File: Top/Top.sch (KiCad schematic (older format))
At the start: 30 parts, among them J1 Conn_01x02_Male, SW1 SW_DPDT_x2, U2 MCP73831-2-OT, U3 SSD1306

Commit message: V0.2: Redo front schematic and PCB
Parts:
- removed H6: VBS, Custom:Mounting_Pad_Power, symbol Custom:MountingPad
- removed SW1: SW_DPDT_x2, Custom:JS102011SAQN, symbol Switch:SW_DPDT_x2
- H12, H13: value VBS -> PWR
- H2: value VSW -> PWR
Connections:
- net VBAT_SWITCH is gone; now on net VBUS: D1.1 (K), H2.1 (Pin)
- net +BATT: now also D1.2 (A)
- no-connect marks 1 -> 0
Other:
- note added: "Iref determines brightness"
- moved on the sheet: C2, D1, D2, H1, H10, H11, H12, H13, H2, H7, H8, H9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

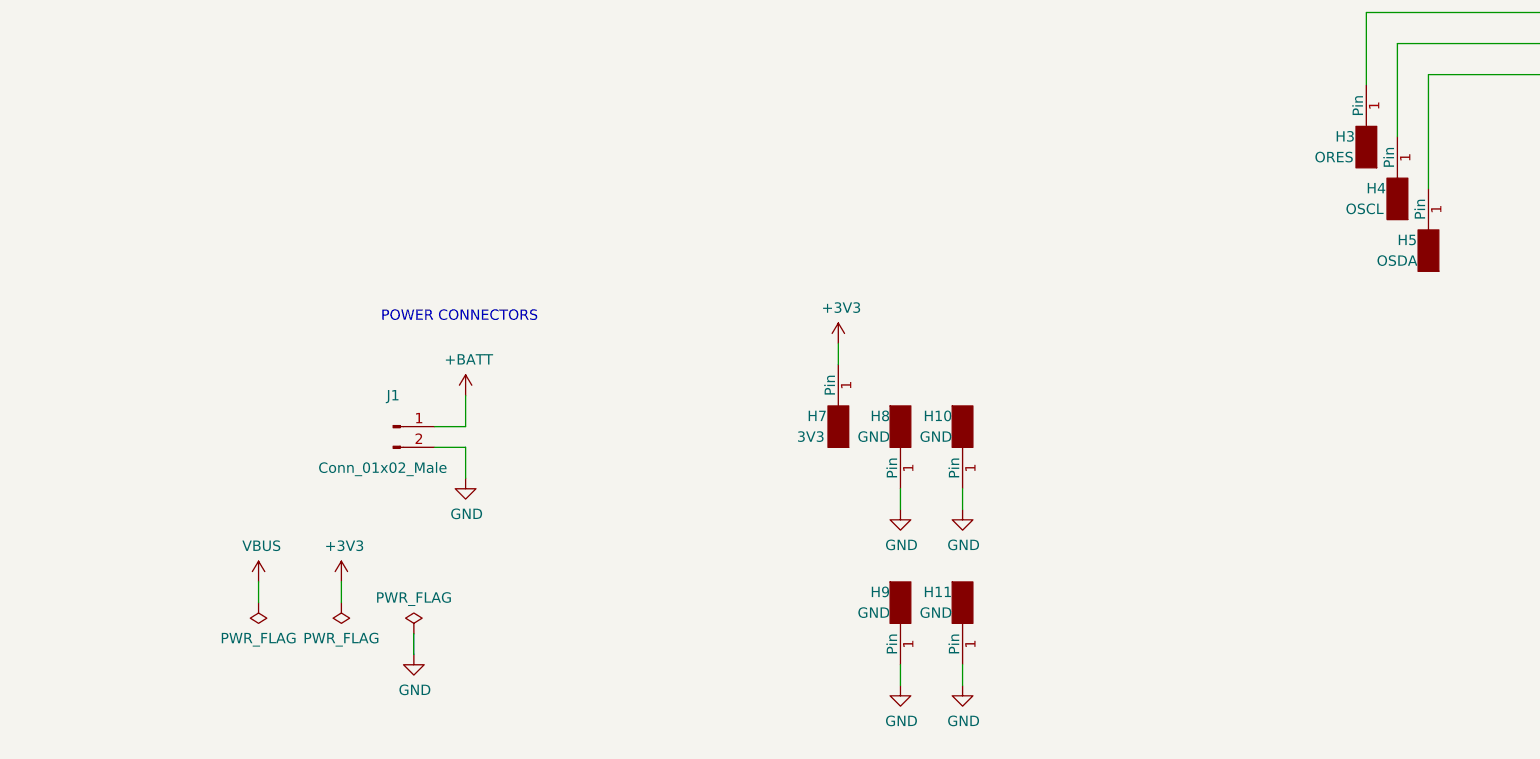
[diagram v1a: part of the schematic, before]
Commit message: updated bottom (motor placement, sharp sensor), front redesign, start op top redesign
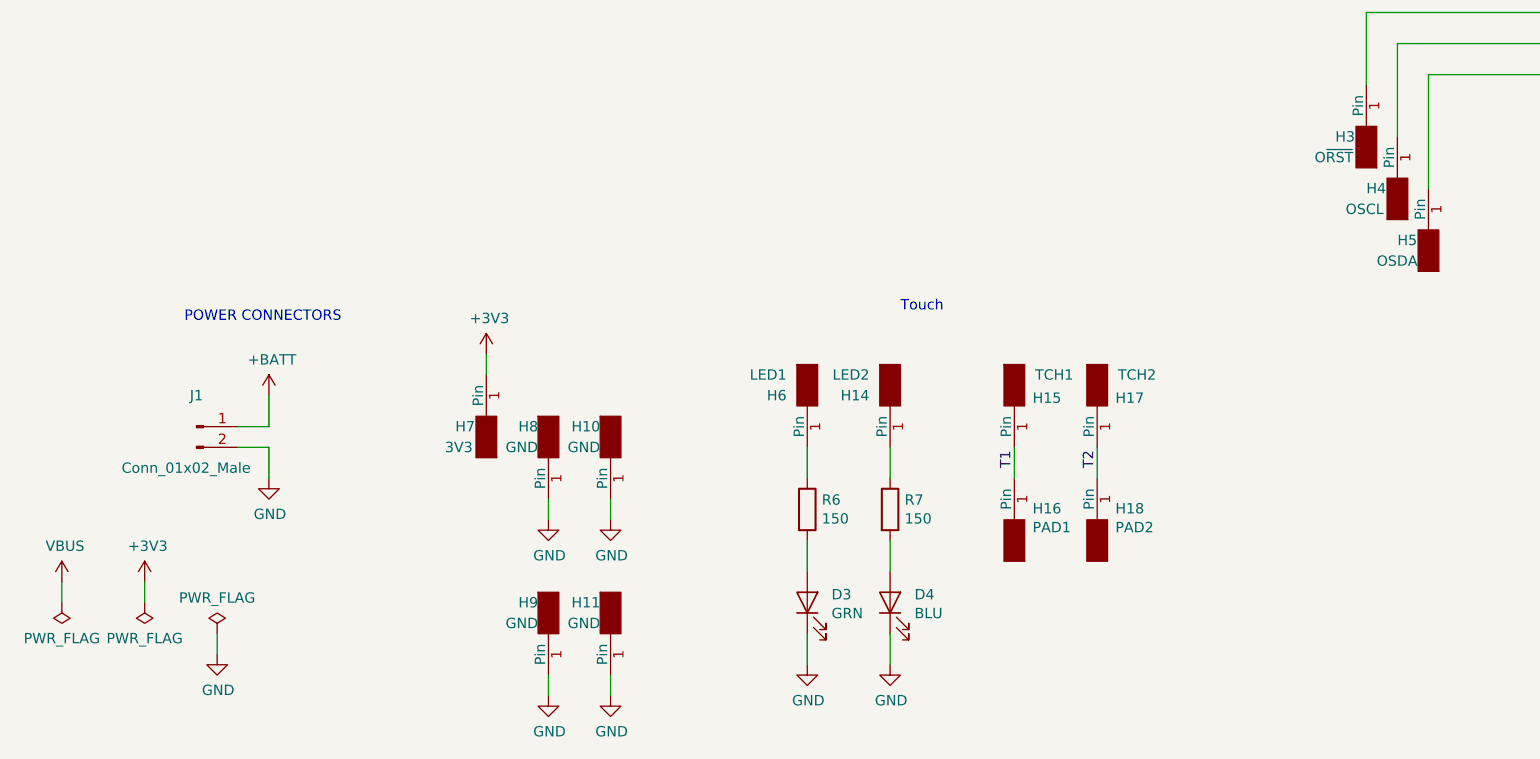
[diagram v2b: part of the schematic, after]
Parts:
- added D3: GRN, LED_SMD:LED_0805_2012Metric, symbol Device:LED
- added D4: BLU, LED_SMD:LED_0805_2012Metric, symbol Device:LED
- added H14: LED2, Custom:Mounting_Pad_Signal, symbol Custom:MountingPad
- added H15: TCH1, Custom:Mounting_Pad_Touch, symbol Custom:MountingPad
- added H16: PAD1, Custom:Touch_Pad, symbol Custom:MountingPad
- added H17: TCH2, Custom:Mounting_Pad_Touch, symbol Custom:MountingPad
- added H18: PAD2, Custom:Touch_Pad, symbol Custom:MountingPad
- added H6: LED1, Custom:Mounting_Pad_Signal, symbol Custom:MountingPad
- added R6, R7: 150, Resistor_SMD:R_0805_2012Metric, symbol Device:R
- H3: value ORES -> O~RST
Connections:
- net GND: now also D3.1 (K), D4.1 (K)
- new net: H6.1 (Pin), R6.1
- new net: H14.1 (Pin), R7.1
- new net: D3.2 (A), R6.2
- new net: D4.2 (A), R7.2
- new net T1: H15.1 (Pin), H16.1 (Pin)
- new net T2: H17.1 (Pin), H18.1 (Pin)
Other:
- note added: "Touch"
- moved on the sheet: H10, H11, H7, H8, H9, J1

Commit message: Update Top V0.2, small changes to motor placement
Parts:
- D2: footprint LED_SMD:LED_0603_1608Metric -> LED_SMD:LED_0805_2012Metric
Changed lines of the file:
@@
 F 0 "D2" V 4289 1782 50  0000 R CNN
 F 1 "ORANGE" V 4198 1782 50  0000 R CNN
-F 2 "LED_SMD:LED_0603_1608Metric" H 4250 1900 50  0001 C CNN
+F 2 "LED_SMD:LED_0805_2012Metric" H 4250 1900 50  0001 C CNN
 F 3 "~" H 4250 1900 50  0001 C CNN
 F 4 "C84269" H 4250 1900 50  0001 C CNN "LCSC"

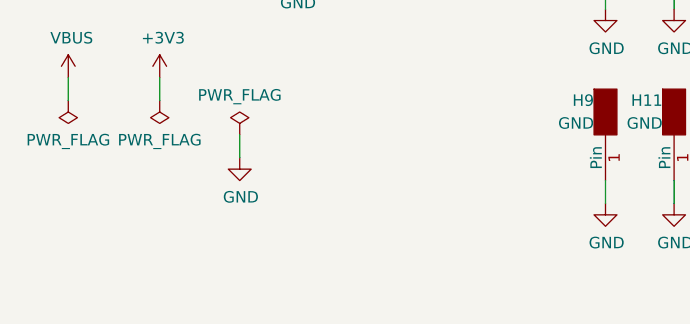
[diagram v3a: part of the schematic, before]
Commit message: finish top, changes to front, added graphic
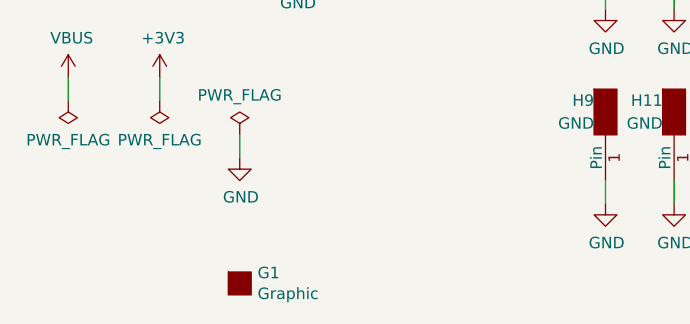
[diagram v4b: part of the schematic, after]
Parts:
- added G1: Graphic, Print:d3, symbol Custom:Graphic
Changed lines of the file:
@@
 Text Label 5950 5950 1    50   ~ 0
 T2
+$Comp
+L Custom:Graphic G1
+U 1 1 5DED0901
+P 1700 7400
+F 0 "G1" H 1778 7446 50  0000 L CNN
+F 1 "Graphic" H 1778 7355 50  0000 L CNN
+F 2 "Print:d3" H 1550 7550 50  0001 C CNN
+F 3 "" H 1550 7550 50  0001 C CNN
+	1    1700 7400
+	1    0    0    -1
+$EndComp
 $EndSCHEMATC
